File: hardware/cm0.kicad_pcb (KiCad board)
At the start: 4 copper layers, 53.2 x 36.4 mm, 12 parts, among them U1 H3, U2 H5TQ4G63EFR

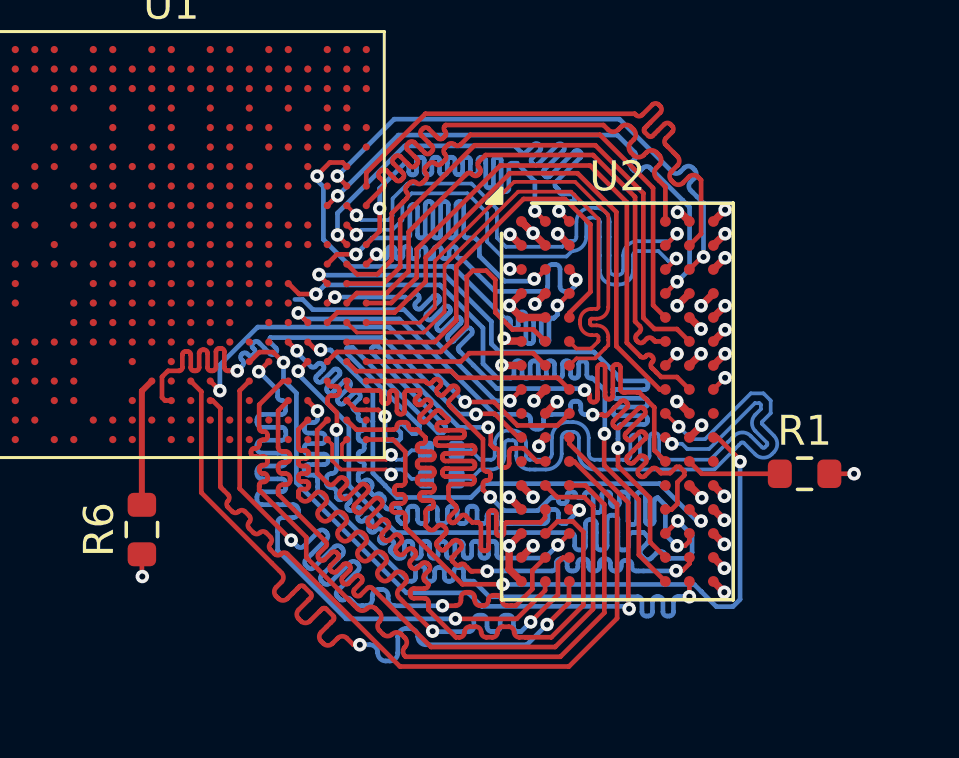
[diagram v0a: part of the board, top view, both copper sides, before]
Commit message: Added A13 line to DDR3
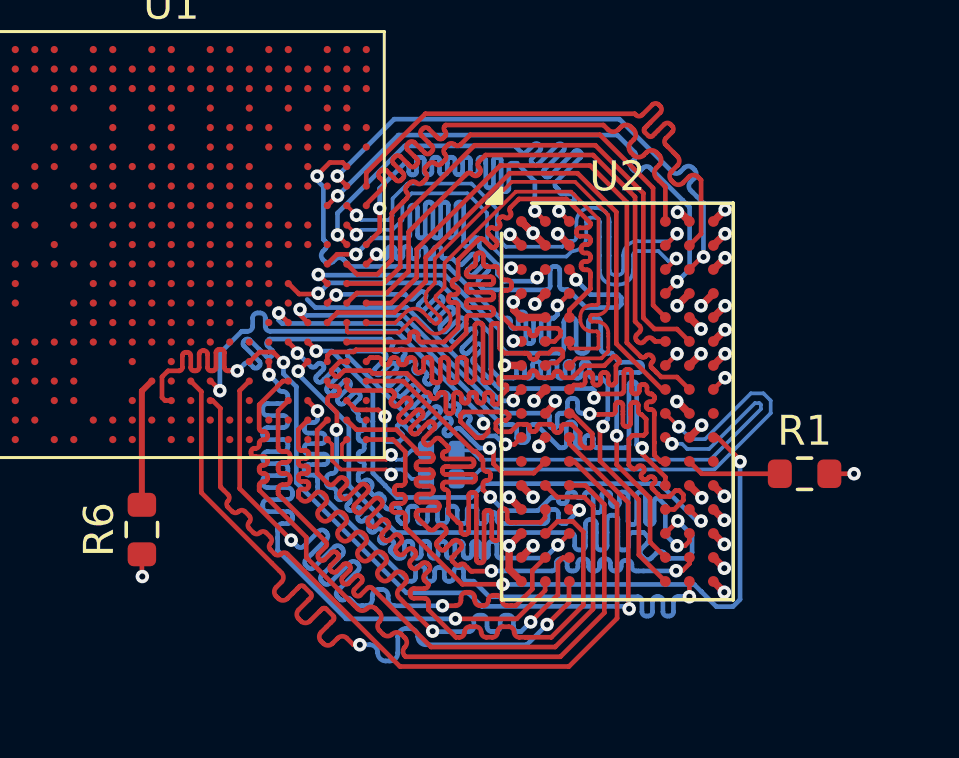
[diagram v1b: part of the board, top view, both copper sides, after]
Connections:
- U1 pad R17: /H3/A15 -> /DDR3/A15
- U2 pad M7: unconnected-(U2-NC-PadM7) -> /DDR3/A15
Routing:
- net /DDR3/A15: track 0.00 -> 23.4 mm, vias 0 -> 2
- net /DDR3/DQ6: track 6.26 -> 19.3 mm
- net /DDR3/DQ4: track 7.81 -> 19.3 mm
- net /DDR3/~{RAS}: track 15.0 -> 23.4 mm
- net /DDR3/DQ2: track 11.1 -> 19.3 mm
- net /DDR3/CLK-: track 22.9 -> 15.1 mm
- net /DDR3/DQ9: track 12.9 -> 17.8 mm
- net /DDR3/CLK+: track 21.2 -> 16.4 mm
- net /DDR3/DQ0: track 14.9 -> 19.2 mm
- net /DDR3/ODT: track 20.1 -> 23.2 mm
- net /DDR3/A4: track 23.3 -> 21.4 mm
- net /DDR3/A12: track 24.8 -> 23.3 mm
- net /DDR3/DQS0+: track 17.8 -> 19.3 mm
- net /DDR3/DQS0-: track 18.1 -> 19.3 mm
- net /DDR3/DQM1: track 17.2 -> 17.8 mm
